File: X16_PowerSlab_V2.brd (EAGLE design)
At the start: 100 x 80 mm, 46 parts, among them J1 CONN_796636-3, J2 CONN_796636-3, J3 CONN_ET60T, U1 LINEAR_AZ1117CR-3.3TRG1DIODES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

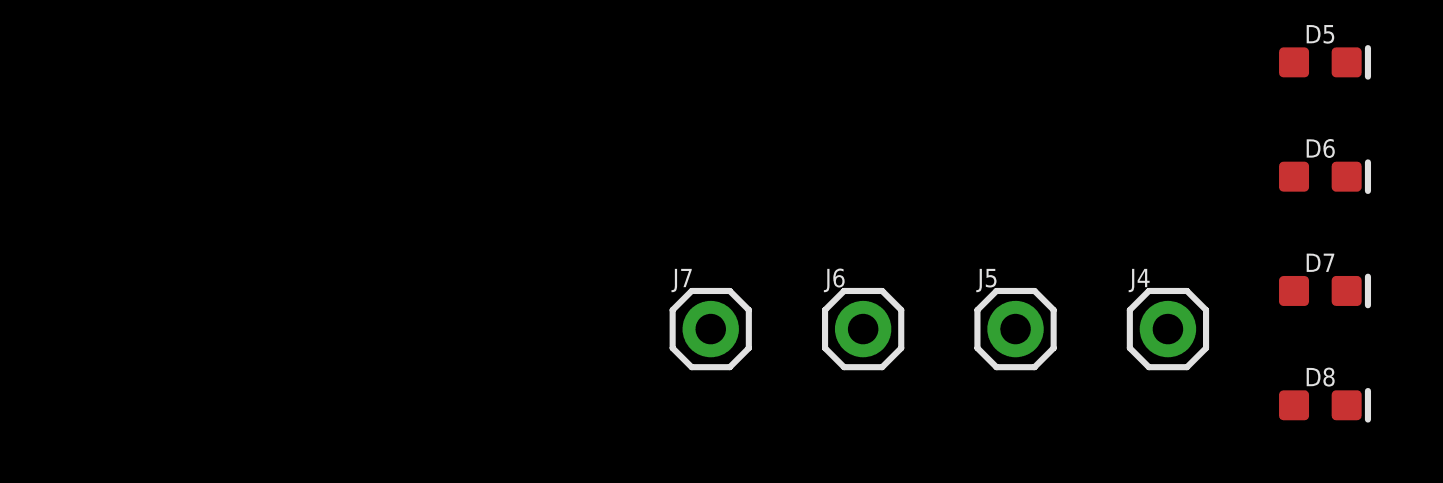
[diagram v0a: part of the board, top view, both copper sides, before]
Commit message: Added testpoints, fixed some errors with values
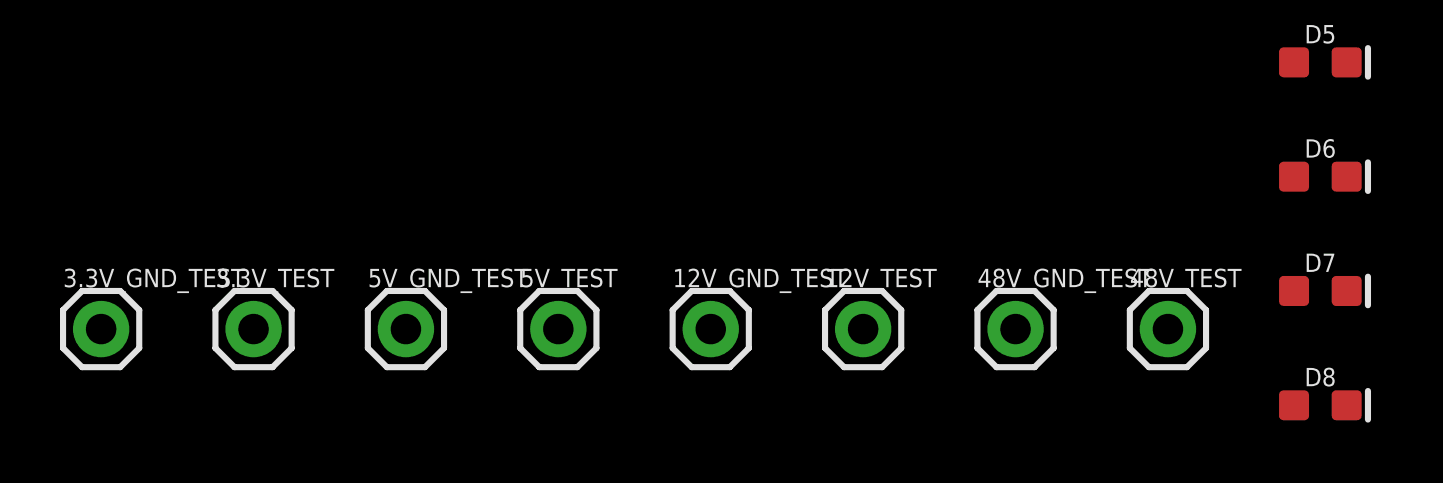
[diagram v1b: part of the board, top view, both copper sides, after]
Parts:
- added 3.3V_GND_TEST, 3.3V_TEST, 5V_GND_TEST, 5V_TEST: (no value), SparkFun-Connectors:1X01
- D5: value (none) -> 48V
- D6: value (none) -> 12V
- D7: value (none) -> 5V
- D8: value (none) -> 3.3V
- renumbered J4 to 48V_TEST, J5 to 48V_GND_TEST, J6 to 12V_TEST, J7 to 12V_GND_TEST
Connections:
- removed net 12_GND: D7.C, D8.C
- new net N$15: 5V_TEST.1
- new net N$16: 5V_GND_TEST.1
- new net N$17: 3.3V_TEST.1
- new net N$18: 3.3V_GND_TEST.1
- net 12V: now also 12V_TEST.1
- net 12V_GND: now also 12V_GND_TEST.1, D7.C, D8.C
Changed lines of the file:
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@@
 <attribute name="VALUE" x="-111.76" y="-163.322" size="0.6096" layer="27" font="vector" ratio="20" align="top-center"/>
 </element>
-<element name="D5" library="SparkFun-LED" library_urn="urn:adsk.eagle:library:529" package="LED-0603" package3d_urn="urn:adsk.eagle:package:39354/2" value="" x="-111.76" y="-204.47" smashed="yes">
+<element name="D5" library="SparkFun-LED" library_urn="urn:adsk.eagle:library:529" package="LED-0603" package3d_urn="urn:adsk.eagle:package:39354/2" value="48V" x="-111.76" y="-204.47" smashed="yes">
 <attribute name="NAME" x="-111.76" y="-203.835" size="0.6096" layer="25" font="vector" ratio="20" align="bottom-center"/>
 <attribute name="VALUE" x="-111.76" y="-205.105" size="0.6096" layer="27" font="vector" ratio="20" align="top-center"/>
 </element>
-<element name="D6" library="SparkFun-LED" library_urn="urn:adsk.eagle:library:529" package="LED-0603" package3d_urn="urn:adsk.eagle:package:39354/2" value="" x="-111.76" y="-208.28" smashed="yes">
+<element name="D6" library="SparkFun-LED" library_urn="urn:adsk.eagle:library:529" package="LED-0603" package3d_urn="urn:adsk.eagle:package:39354/2" value="12V" x="-111.76" y="-208.28" smashed="yes">
 <attribute name="NAME" x="-111.76" y="-207.645" size="0.6096" layer="25" font="vector" ratio="20" align="bottom-center"/>
 <attribute name="VALUE" x="-111.76" y="-208.915" size="0.6096" layer="27" font="vector" ratio="20" align="top-center"/>
 </element>
-<element name="D7" library="SparkFun-LED" library_urn="urn:adsk.eagle:library:529" package="LED-0603" package3d_urn="urn:adsk.eagle:package:39354/2" value="" x="-111.76" y="-212.09" smashed="yes">
+<element name="D7" library="SparkFun-LED" library_urn="urn:adsk.eagle:library:529" package="LED-0603" package3d_urn="urn:adsk.eagle:package:39354/2" value="5V" x="-111.76" y="-212.09" smashed="yes">
 <attribute name="NAME" x="-111.76" y="-211.455" size="0.6096" layer="25" font="vector" ratio="20" align="bottom-center"/>
 <attribute name="VALUE" x="-111.76" y="-212.725" size="0.6096" layer="27" font="vector" ratio="20" align="top-center"/>
 </element>
-<element name="D8" library="SparkFun-LED" library_urn="urn:adsk.eagle:library:529" package="LED-0603" package3d_urn="urn:adsk.eagle:package:39354/2" value="" x="-111.76" y="-215.9" smashed="yes">
+<element name="D8" library="SparkFun-LED" library_urn="urn:adsk.eagle:library:529" package="LED-0603" package3d_urn="urn:adsk.eagle:package:39354/2" value="3.3V" x="-111.76" y="-215.9" smashed="yes">
 <attribute name="NAME" x="-111.76" y="-215.265" size="0.6096" layer="25" font="vector" ratio="20" align="bottom-center"/>
 <attribute name="VALUE" x="-111.76" y="-216.535" size="0.6096" layer="27" font="vector" ratio="20" align="top-center"/>
 </element>
-<element name="J4" library="SparkFun-Connectors" library_urn="urn:adsk.eagle:library:513" package="1X01" package3d_urn="urn:adsk.eagle:package:38028/2" value="" x="-116.84" y="-213.36" smashed="yes">
+<element name="48V_TEST" library="SparkFun-Connectors" library_urn="urn:adsk.eagle:library:513" package="1X01" package3d_urn="urn:adsk.eagle:package:38028/2" value="" x="-116.84" y="-213.36" smashed="yes">
 <attribute name="NAME" x="-118.11" y="-211.963" size="0.6096" layer="25" font="vector" ratio="20"/>
 <attribute name="VALUE" x="-118.11" y="-214.884" size="0.6096" layer="27" font="vector" ratio="20" align="top-left"/>
 </element>
-<element name="J5" library="SparkFun-Connectors" library_urn="urn:adsk.eagle:library:513" package="1X01" package3d_urn="urn:adsk.eagle:package:38028/2" value="" x="-121.92" y="-213.36" smashed="yes">
+<element name="48V_GND_TEST" library="SparkFun-Connectors" library_urn="urn:adsk.eagle:library:513" package="1X01" package3d_urn="urn:adsk.eagle:package:38028/2" value="" x="-121.92" y="-213.36" smashed="yes">
 <attribute name="NAME" x="-123.19" y="-211.963" size="0.6096" layer="25" font="vector" ratio="20"/>
 <attribute name="VALUE" x="-123.19" y="-214.884" size="0.6096" layer="27" font="vector" ratio="20" align="top-left"/>
 </element>
-<element name="J6" library="SparkFun-Connectors" library_urn="urn:adsk.eagle:library:513" package="1X01" package3d_urn="urn:adsk.eagle:package:38028/2" value="" x="-127" y="-213.36" smashed="yes">
+<element name="12V_TEST" library="SparkFun-Connectors" library_urn="urn:adsk.eagle:library:513" package="1X01" package3d_urn="urn:adsk.eagle:package:38028/2" value="" x="-127" y="-213.36" smashed="yes">
 <attribute name="NAME" x="-128.27" y="-211.963" size="0.6096" layer="25" font="vector" ratio="20"/>
 <attribute name="VALUE" x="-128.27" y="-214.884" size="0.6096" layer="27" font="vector" ratio="20" align="top-left"/>
 </element>
-<element name="J7" library="SparkFun-Connectors" library_urn="urn:adsk.eagle:library:513" package="1X01" package3d_urn="urn:adsk.eagle:package:38028/2" value="" x="-132.08" y="-213.36" smashed="yes">
+<element name="12V_GND_TEST" library="SparkFun-Connectors" library_urn="urn:adsk.eagle:library:513" package="1X01" package3d_urn="urn:adsk.eagle:package:38028/2" value="" x="-132.08" y="-213.36" smashed="yes">
 <attribute name="NAME" x="-133.35" y="-211.963" size="0.6096" layer="25" font="vector" ratio="20"/>
 <attribute name="VALUE" x="-133.35" y="-214.884" size="0.6096" layer="27" font="vector" ratio="20" align="top-left"/>
+</element>
+<element name="5V_TEST" library="SparkFun-Connectors" library_urn="urn:adsk.eagle:library:513" package="1X01" package3d_urn="urn:adsk.eagle:package:38028/2" value="" x="-137.16" y="-213.36" smashed="yes">
+<attribute name="NAME" x="-138.43" y="-211.963" size="0.6096" layer="25" font="vector" ratio="20"/>
+<attribute name="VALUE" x="-138.43" y="-214.884" size="0.6096" layer="27" font="vector" ratio="20" align="top-left"/>
+</element>
+<element name="5V_GND_TEST" library="SparkFun-Connectors" library_urn="urn:adsk.eagle:library:513" package="1X01" package3d_urn="urn:adsk.eagle:package:38028/2" value="" x="-142.24" y="-213.36" smashed="yes">
+<attribute name="NAME" x="-143.51" y="-211.963" size="0.6096" layer="25" font="vector" ratio="20"/>
+<attribute name="VALUE" x="-143.51" y="-214.884" size="0.6096" layer="27" font="vector" ratio="20" align="top-left"/>
+</element>
+<element name="3.3V_TEST" library="SparkFun-Connectors" library_urn="urn:adsk.eagle:library:513" package="1X01" package3d_urn="urn:adsk.eagle:package:38028/2" value="" x="-147.32" y="-213.36" smashed="yes">
+<attribute name="NAME" x="-148.59" y="-211.963" size="0.6096" layer="25" font="vector" ratio="20"/>
+<attribute name="VALUE" x="-148.59" y="-214.884" size="0.6096" layer="27" font="vector" ratio="20" align="top-left"/>
+</element>
+<element name="3.3V_GND_TEST" library="SparkFun-Connectors" library_urn="urn:adsk.eagle:library:513" package="1X01" package3d_urn="urn:adsk.eagle:package:38028/2" value="" x="-152.4" y="-213.36" smashed="yes">
+<attribute name="NAME" x="-153.67" y="-211.963" size="0.6096" layer="25" font="vector" ratio="20"/>
+<attribute name="VALUE" x="-153.67" y="-214.884" size="0.6096" layer="27" font="vector" ratio="20" align="top-left"/>
 </element>
 </elements>
@@
 <contactref element="R4" pad="2"/>
 <contactref element="R8" pad="1"/>
-<contactref element="J4" pad="1"/>
+<contactref element="48V_TEST" pad="1"/>
 <wire x1="-112.61" y1="-151.13" x2="-100.2157" y2="-132.08" width="0" layer="19" extent="1-1"/>
 <wire x1="-100.2157" y1="-104.14" x2="-100.2157" y2="-132.08" width="0" layer="19" extent="1-1"/>
@@
 <contactref element="D1" pad="A"/>
 <contactref element="D5" pad="C"/>
-<contactref element="J5" pad="1"/>
+<contactref element="48V_GND_TEST" pad="1"/>
 <wire x1="-90.2843" y1="-104.14" x2="-90.2843" y2="-132.08" width="0" layer="19" extent="1-1"/>
 <wire x1="-90.2843" y1="-76.2" x2="-90.2843" y2="-104.14" width="0" layer="19" extent="1-1"/>
@@
 <signal name="12V">
 <contactref element="R9" pad="1"/>
+<contactref element="12V_TEST" pad="1"/>
+<wire x1="-112.61" y1="-154.94" x2="-127" y2="-213.36" width="0" layer="19" extent="1-1"/>
 </signal>
 <signal name="12V_GND">
 <contactref element="D6" pad="C"/>
+<contactref element="12V_GND_TEST" pad="1"/>
+<contactref element="D7" pad="C"/>
+<contactref element="D8" pad="C"/>
+<wire x1="-110.883" y1="-212.09" x2="-132.08" y2="-213.36" width="0" layer="19" extent="1-1"/>
+<wire x1="-110.883" y1="-215.9" x2="-110.883" y2="-212.09" width="0" layer="19" extent="1-1"/>
+<wire x1="-110.883" y1="-208.28" x2="-110.883" y2="-212.09" width="0" layer="19" extent="1-1"/>
 </signal>
 <signal name="5V">
 <contactref element="R10" pad="1"/>
 </signal>
-<signal name="12_GND">
-<contactref element="D7" pad="C"/>
-<contactref element="D8" pad="C"/>
-<wire x1="-110.883" y1="-212.09" x2="-110.883" y2="-215.9" width="0" layer="19" extent="1-1"/>
-</signal>
 <signal name="3.3V">
 <contactref element="R11" pad="1"/>
@@
 <contactref element="U$6" pad="PIN3"/>
 </signal>
+<signal name="N$15">
+<contactref element="5V_TEST" pad="1"/>
+</signal>
+<signal name="N$16">
+<contactref element="5V_GND_TEST" pad="1"/>
+</signal>
+<signal name="N$17">
+<contactref element="3.3V_TEST" pad="1"/>
+</signal>
+<signal name="N$18">
+<contactref element="3.3V_GND_TEST" pad="1"/>
+</signal>
 </signals>

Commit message: schematic finished
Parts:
- removed 3.3V_GND_TEST, 3.3V_TEST: (no value), SparkFun-Connectors:1X01
- removed C3: 10uF, SparkFun-Capacitors:0603
- removed C4: 22uF, SparkFun-Capacitors:0603
- removed D4, D8: 3.3V, SparkFun-LED:LED-0603
- removed R11: 0.1, SparkFun-Resistors:0603
- removed R7: (no value), SparkFun-Resistors:0603
- removed U$6: CONN_BMR480_BRICK, X16_Power_Slab:CONN_BMR480_BRICK
- removed U1: LINEAR_AZ1117CR-3.3TRG1DIODES_AZ1117CH-3.3TRG1_0_0, X16_Power_Slab:LINEAR_AZ1117CR-3.3TRG1
- U$3: value 3.3V_TESTPOINT -> CONN_BMR480_BRICK; device X15-Conversion-Parts-Library:3.3V_TESTPOINT -> X16_Power_Slab:CONN_BMR480_BRICK
- moved U$3 391.2 mm to (-142.2, -256.5)
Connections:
- removed net 12V/1.1B: R5.1, U$5.12V
- removed net 12V/2.1A: CIN1.+, CIN2.1, U$2.PIN2
- removed net 3.3V: R11.1
- removed net 3.3V/1.4C: R7.1, U$3.3.3V
- removed net 3.3V/2.1B: C4.1, U1.2, U1.4
- removed net 5.2V/1.5B: R6.1, U$4.5.2V
- removed net 5.2V/2.1A: C3.1, COUT1.+, COUT2.+, COUT3.+, L1.2, R2.2, U1.3
- removed net GND/1.5A: D2.C, D3.C, D4.C
- removed net GND/2.2D: C3.2, C4.2, CIN1.-, CIN2.2, COUT1.-, COUT2.-, COUT3.-, DIODE.A, R3.1, U$2.PIN4, U$2.PIN8, U1.1
- removed net N$12: D8.A, R11.2
- removed net N$13: U$6.PIN1
- removed net N$14: U$6.PIN5
- removed net N$15: 5V_TEST.1
- removed net N$16: 5V_GND_TEST.1
- removed net N$17: 3.3V_TEST.1
- removed net N$18: 3.3V_GND_TEST.1
- removed net N$19: U$6.PIN4
- removed net N$20: U$6.PIN8
- removed net N$21: U$6.PIN7
- removed net N$22: U$6.PIN3
- removed net N$6: D4.A, R7.2
- removed net P01: J3.P01_1, J3.P01_10, J3.P01_2, J3.P01_3, J3.P01_4, J3.P01_5, J3.P01_6, J3.P01_7, J3.P01_8, J3.P01_9
- removed net P02: J3.P02_1, J3.P02_10, J3.P02_2, J3.P02_3, J3.P02_4, J3.P02_5, J3.P02_6, J3.P02_7, J3.P02_8, J3.P02_9
- removed net P03: J3.P03_1, J3.P03_10, J3.P03_2, J3.P03_3, J3.P03_4, J3.P03_5, J3.P03_6, J3.P03_7, J3.P03_8, J3.P03_9
- removed net P04: J3.P04_1, J3.P04_10, J3.P04_2, J3.P04_3, J3.P04_4, J3.P04_5, J3.P04_6, J3.P04_7, J3.P04_8, J3.P04_9
- removed net P05: J3.P05_1, J3.P05_10, J3.P05_2, J3.P05_3, J3.P05_4, J3.P05_5, J3.P05_6, J3.P05_7, J3.P05_8, J3.P05_9
- removed net P06: J3.P06_1, J3.P06_10, J3.P06_2, J3.P06_3, J3.P06_4, J3.P06_5, J3.P06_6, J3.P06_7, J3.P06_8, J3.P06_9
- removed net P07: J3.P07_1, J3.P07_10, J3.P07_2, J3.P07_3, J3.P07_4, J3.P07_5, J3.P07_6, J3.P07_7, J3.P07_8, J3.P07_9
- removed net P08: J3.P08_1, J3.P08_10, J3.P08_2, J3.P08_3, J3.P08_4, J3.P08_5, J3.P08_6, J3.P08_7, J3.P08_8, J3.P08_9
- new net 5.2V: 5V_TEST.1, COUT1.+, COUT2.+, COUT3.+, L1.2, R2.2, R6.1, U$4.5.2V
- new net PMBUS_CTRL: J3.17, U$3.PIN9
- new net PMBUS_GND: J3.18, U$3.PIN10
- new net PMBUS_SA0: J3.22, U$3.PIN15
- new net PMBUS_SA1: J3.23, U$3.PIN14
- new net PMBUS_SALERT: J3.20, U$3.PIN12
- new net PMBUS_SCL: J3.21, U$3.PIN13
- new net PMBUS_SDA: J3.19, U$3.PIN11
- net 12V: now also CIN1.+, CIN2.1, J3.P01_1, J3.P01_10, J3.P01_2, J3.P01_3, J3.P01_4, J3.P01_5, J3.P01_6, J3.P01_7, J3.P01_8, J3.P01_9, J3.P02_1, J3.P02_10, J3.P02_2, J3.P02_3, J3.P02_4, J3.P02_5, J3.P02_6, J3.P02_7, J3.P02_8, J3.P02_9, R5.1, U$2.PIN2, U$3.PIN7, U$3.PIN8, U$5.12V
- net 12V_GND: now also J3.P03_1, J3.P03_10, J3.P03_2, J3.P03_3, J3.P03_4, J3.P03_5, J3.P03_6, J3.P03_7, J3.P03_8, J3.P03_9, J3.P04_1, J3.P04_10, J3.P04_2, J3.P04_3, J3.P04_4, J3.P04_5, J3.P04_6, J3.P04_7, J3.P04_8, J3.P04_9; no longer 12V_GND_TEST.1, D6.C, D7.C, D8.C
- net 48V: now also U$3.PIN1
- net 48V_GND: now also U$3.PIN3
- net 5V: now also J3.P05_1, J3.P05_10, J3.P05_2, J3.P05_3, J3.P05_4, J3.P05_5, J3.P05_6, J3.P05_7, J3.P05_8, J3.P05_9, J3.P06_1, J3.P06_10, J3.P06_2, J3.P06_3, J3.P06_4, J3.P06_5, J3.P06_6, J3.P06_7, J3.P06_8, J3.P06_9
- net GND: now also 12V_GND_TEST.1, 5V_GND_TEST.1, CIN1.-, CIN2.2, COUT1.-, COUT2.-, COUT3.-, D2.C, D3.C, D6.C, D7.C, DIODE.A, J3.P07_1, J3.P07_10, J3.P07_2, J3.P07_3, J3.P07_4, J3.P07_5, J3.P07_6, J3.P07_7, J3.P07_8, J3.P07_9, J3.P08_1, J3.P08_10, J3.P08_2, J3.P08_3, J3.P08_4, J3.P08_5, J3.P08_6, J3.P08_7, J3.P08_8, J3.P08_9, R3.1, U$2.PIN4, U$2.PIN8, U$3.PIN4, U$3.PIN5; no longer J2.1, J2.2, J2.3
- net GND_RAW: now also J2.1, J2.2, J2.3

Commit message: Fixed area of board
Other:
- board size 100 x 80 mm -> 152.4 x 76.2 mm
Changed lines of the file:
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@@
 <board>
 <plain>
-<wire x1="0" y1="0" x2="100" y2="0" width="0" layer="20"/>
-<wire x1="100" y1="0" x2="100" y2="80" width="0" layer="20"/>
-<wire x1="100" y1="80" x2="0" y2="80" width="0" layer="20"/>
-<wire x1="0" y1="80" x2="0" y2="0" width="0" layer="20"/>
+<wire x1="-0.4064" y1="0.762" x2="151.9936" y2="0.762" width="0" layer="20"/>
+<wire x1="151.9936" y1="0.762" x2="151.9936" y2="61.722" width="0" layer="20"/>
+<wire x1="-0.4064" y1="64.262" x2="-0.4064" y2="0.762" width="0" layer="20"/>
+<wire x1="136.7536" y1="76.962" x2="136.7536" y2="61.722" width="0" layer="20"/>
+<wire x1="136.7536" y1="61.722" x2="151.9936" y2="61.722" width="0" layer="20"/>
+<wire x1="12.2936" y1="76.962" x2="136.7536" y2="76.962" width="0" layer="20"/>
+<wire x1="12.2936" y1="76.962" x2="-0.4064" y2="64.262" width="0" layer="20" curve="90"/>
 </plain>
 <attributes>

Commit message: Started placing components on board
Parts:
- moved U$3 381.9 mm to (73.7, 58.4), turned to 180 degrees
- moved J3 164.1 mm to (67.3, 8.89)
- moved U$1 137.2 mm to (12.7, 10.2), turned to 180 degrees
- moved J2 98.3 mm to (6.35, 22.9), turned to 90 degrees
- moved J1 48.4 mm to (6.35, 43.2), turned to 90 degrees
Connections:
- removed net 5.2V: 5V_TEST.1, COUT1.+, COUT2.+, COUT3.+, L1.2, R2.2, R6.1, U$4.5.2V
- net 5V: now also 5V_TEST.1, COUT1.+, COUT2.+, COUT3.+, L1.2, R2.2, R6.1, U$4.5.2V

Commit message: Started placing board components
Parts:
- removed C1, C5, C6: 330uF, X15_Brickstribution:CAP_099112E3_VIS-M
- removed R3: (no value), SparkFun-Resistors:0603
- added C3, C4, C7: 330uF, SparkFun-Capacitors:0603-POLAR
- added CR1: DIODE(Z)_SMBJ5357B-TPDIODE_DO-214AA_4P38X3P62_MCC-M, X15_Brickstribution:DIODE_DO-214AA_4P38X3P62_MCC-M
- added D4: 250mA/100V, SparkFun-DiscreteSemi:SOD-323
- added RADJ: 12.4k, SparkFun-Resistors:0603
- D7: value 5V -> 5.2V
- R1: value (none) -> 1k
- R10: value 0.1 -> 100
- R2: value (none) -> 3.32k
- R4: value (none) -> 1M
- R5: value (none) -> 600
- R6: value (none) -> 300
- moved 12V_TEST 335.0 mm to (114.3, 19.1), turned to 270 degrees
- moved D6 320.1 mm to (102.9, 29.2), turned to 90 degrees
- moved D7 316.2 mm to (106.7, 16.5)
- moved 48V_GND_TEST 305.0 mm to (14.0, 59.7)
- moved D5 290.4 mm to (8.89, 59.7)
- moved R9 283.3 mm to (106.7, 25.4), turned to 90 degrees
- moved R10 255.5 mm to (86.4, 2.54)
- moved R8 246.0 mm to (1.27, 67.3)
- moved D3 244.9 mm to (102.9, 33.9), turned to 270 degrees
- moved D2 233.6 mm to (106.7, 32.1), turned to 90 degrees
- moved COUT3 224.5 mm to (121.9, 35.6), turned to 90 degrees
- moved COUT2 223.0 mm to (121.9, 30.5), turned to 90 degrees
- moved COUT1 221.6 mm to (121.9, 25.4), turned to 90 degrees
- moved CIN1 213.0 mm to (115.6, 24.1), turned to 270 degrees
- moved C2 205.3 mm to (94.0, 36.8), turned to 90 degrees
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- renumbered 5V_GND_TEST to 5.2V_GND_TEST, 5V_TEST to 5.2V_TEST
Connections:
- net 5V renamed 5.2V
- net 12V: now also CR1.1, D4.A, D4.C
- net 48V: now also C3.+, C4.+, C7.+; no longer C1.1, C5.1, C6.1
- net 48V_GND: now also C3.-, C4.-, C7.-; no longer C1.2, C5.2, C6.2
- net GND: now also CR1.2, RADJ.1; no longer R3.1
- net N$8: now also RADJ.2; no longer R3.2

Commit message: all components laid out
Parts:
- moved C7 354.8 mm to (40.6, 61.0)
- moved C4 348.9 mm to (35.6, 61.0)
- moved 5.2V_GND_TEST 344.7 mm to (124.5, 5.08)
- moved 12V_GND_TEST 340.8 mm to (129.5, 5.08)
- moved 48V_TEST 318.9 mm to (45.7, 61.0)
- moved 5.2V_TEST 308.0 mm to (82.5, 2.54)
- moved R8 8.03 mm to (3.81, 59.7)
